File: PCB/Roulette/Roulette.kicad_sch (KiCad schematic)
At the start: 277 parts, among them J1 USB-PROG, J2 Shelly, J3 Conn_01x03, J3 JST-PH-SM3-TBT, J4 Conn_01x02, J6 C3001289, Q1 C179347, Q4 CJ2301, SW1 SW_Push, U2 ESP32-S3-MINI-1, U2 ME6211C33M5G-N, U5 TP4054

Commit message: New boards
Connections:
- net VBUS: now also J1.1 (VBUS)
- no-connect marks 28 -> 27
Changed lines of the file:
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@@
   (no_connect (at 236.855 50.8))
   (no_connect (at 215.9 139.065))
-  (no_connect (at 174.625 107.315))
   (no_connect (at 212.725 80.645))
   (no_connect (at 267.335 60.96))
@@
         )
       )
+    )
+  )
+  (symbol (lib_id "power:VBUS") (at 174.625 107.315 270) (unit 1)
+    (in_bom yes) (on_board yes) (dnp no)
+    (property "Reference" "#PWR043" (at 170.815 107.315 0)
+      (effects (font (size 1.27 1.27)) hide)
+    )
+    (property "Value" "VBUS" (at 179.959 107.315 90)
+      (effects (font (size 1.27 1.27)))
+    )
+    (property "Footprint" "" (at 174.625 107.315 0)
+      (effects (font (size 1.27 1.27)) hide)
+    )
+    (property "Datasheet" "" (at 174.625 107.315 0)
+      (effects (font (size 1.27 1.27)) hide)
+    )
+    (pin "1")
+    (instances
+      (project "Watchy"
+        (path "/03039abc-65dd-445c-a352-9e386e1f31aa"
+          (reference "#PWR043") (unit 1)
+        )
+      )
+      (project "Roulette"
+        (path "/46c350bb-7de4-4e81-aafd-4af55e37aab0"
+          (reference "#PWR051") (unit 1)
+        )
+      )

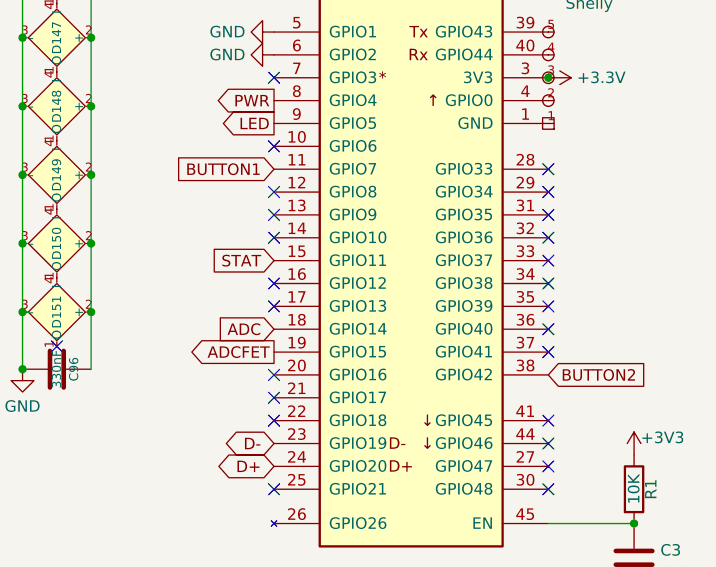
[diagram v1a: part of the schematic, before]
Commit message: Correct btn2
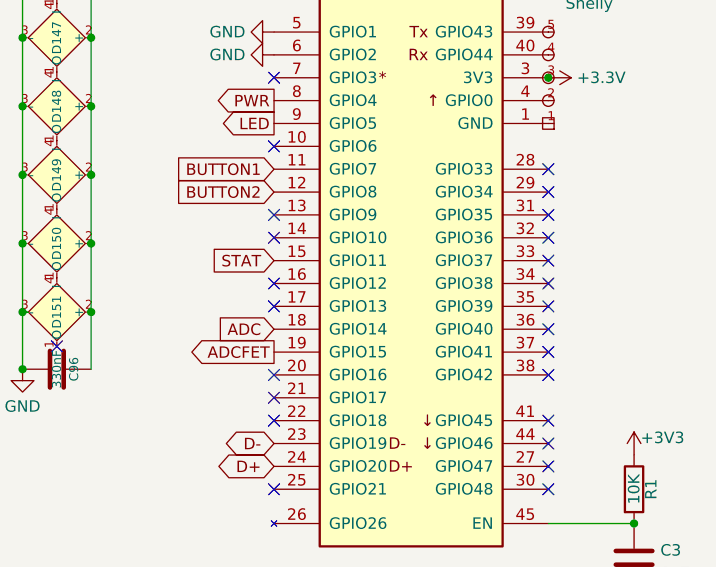
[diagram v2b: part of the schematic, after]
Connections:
- net BUTTON2: now also U2.12 (GPIO8); no longer U2.38 (GPIO42)
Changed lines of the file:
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@@
   (no_connect (at 267.335 66.04))
   (no_connect (at 267.335 78.74))
-  (no_connect (at 236.855 63.5))
+  (no_connect (at 267.335 83.82))
   (wire (pts (xy 208.915 38.735) (xy 208.915 46.355))
     (stroke (width 0) (type default))
@@
     )
   )
-  (global_label "BUTTON2" (shape input) (at 267.335 83.82 0) (fields_autoplaced)
-    (effects (font (size 1.27 1.27)) (justify left))
-    (property "Intersheetrefs" "${INTERSHEET_REFS}" (at 278.0722 83.82 0)
-      (effects (font (size 1.27 1.27)) (justify left) hide)
-    )
-  )
+  (global_label "BUTTON2" (shape input) (at 236.855 63.5 180) (fields_autoplaced)
+    (effects (font (size 1.27 1.27)) (justify right))
+    (property "Intersheetrefs" "${INTERSHEET_REFS}" (at 226.1178 63.5 0)
+      (effects (font (size 1.27 1.27)) (justify right) hide)
+    )
+  )

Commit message: Part IDs
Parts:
- removed J6: C3001289, RevK:USB_C_G_Switch-7082A, symbol RevK:USB_C_Receptacle_G_Switch_7082C
- added J6: USB-C-Socket-V, RevK:USB_C_G_Switch-7082A, symbol RevK:USB-C-Socket-V
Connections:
- net D+: now also J6.A6 (D+), J6.B6 (D+)
- net D-: now also J6.A7 (D-), J6.B7 (D-)
- net GND: now also J6.A1 (GND), J6.A12 (GND), J6.B1 (GND), J6.B12 (GND), J6.S1 (SHIELD)
- net VBUS: now also J6.A4 (VBUS), J6.A9 (VBUS), J6.B4 (VBUS), J6.B9 (VBUS)
- net at R1.2: now also J6.B5 (CC2)
- net at R1.2: now also J6.A5 (CC1)
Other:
- moved on the sheet: R1
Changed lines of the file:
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@@
   (junction (at 31.75 31.115) (diameter 0) (color 0 0 0 0)
   )
+  (junction (at 196.85 148.59) (diameter 0) (color 0 0 0 0)
+  )
   (junction (at 178.435 76.835) (diameter 0) (color 0 0 0 0)
   )
@@
   (junction (at 178.435 24.765) (diameter 0) (color 0 0 0 0)
   )
-  (junction (at 223.52 122.555) (diameter 0) (color 0 0 0 0)
+  (junction (at 223.52 116.84) (diameter 0) (color 0 0 0 0)
   )
   (junction (at -3.175 88.265) (diameter 0) (color 0 0 0 0)
@@
     (stroke (width 0) (type default))
   )
-  (wire (pts (xy 215.9 127.635) (xy 215.9 130.175))
-    (stroke (width 0) (type default))
-  )
   (wire (pts (xy 16.51 28.575) (xy 16.51 33.655))
     (stroke (width 0) (type default))
@@
     (stroke (width 0) (type default))
   )
+  (wire (pts (xy 193.04 148.59) (xy 196.85 148.59))
+    (stroke (width 0) (type default))
+  )
   (wire (pts (xy 24.13 75.565) (xy 24.13 81.915))
     (stroke (width 0) (type default))
@@
     (stroke (width 0) (type default))
   )
-  (wire (pts (xy 215.9 132.715) (xy 215.9 135.255))
-    (stroke (width 0) (type default))
-  )
   (wire (pts (xy 12.7 31.115) (xy 12.7 37.465))
     (stroke (width 0) (type default))
@@
     (stroke (width 0) (type default))
   )
-  (wire (pts (xy 223.52 122.555) (xy 223.52 123.825))
+  (wire (pts (xy 223.52 116.84) (xy 223.52 118.11))
     (stroke (width 0) (type default))
   )
@@
     (stroke (width 0) (type default))
   )
-  (wire (pts (xy 223.52 121.285) (xy 223.52 122.555))
+  (wire (pts (xy 223.52 115.57) (xy 223.52 116.84))
     (stroke (width 0) (type default))
   )
@@
     (stroke (width 0) (type default))
   )
+  (wire (pts (xy 196.85 148.59) (xy 200.66 148.59))
+    (stroke (width 0) (type default))
+  )
   (wire (pts (xy 94.615 46.355) (xy 94.615 53.975))
     (stroke (width 0) (type default))
@@
     )
   )
-  (global_label "D+" (shape bidirectional) (at 215.9 133.985 0) (fields_autoplaced)
+  (global_label "D+" (shape bidirectional) (at 215.9 128.27 0) (fields_autoplaced)
     (effects (font (size 1.27 1.27)) (justify left))
-    (property "Intersheetrefs" "${INTERSHEET_REFS}" (at 221.9465 133.985 0)
+    (property "Intersheetrefs" "${INTERSHEET_REFS}" (at 221.9465 128.27 0)
       (effects (font (size 1.27 1.27)) (justify left) hide)
     )
@@
     )
   )
-  (global_label "D-" (shape bidirectional) (at 215.9 128.905 0) (fields_autoplaced)
+  (global_label "D-" (shape bidirectional) (at 215.9 125.73 0) (fields_autoplaced)
     (effects (font (size 1.27 1.27)) (justify left))
-    (property "Intersheetrefs" "${INTERSHEET_REFS}" (at 221.9465 128.905 0)
+    (property "Intersheetrefs" "${INTERSHEET_REFS}" (at 221.9465 125.73 0)
       (effects (font (size 1.27 1.27)) (justify left) hide)
     )
@@
     )
   )
-  (symbol (lib_id "power:GND") (at 223.52 122.555 90) (unit 1)
+  (symbol (lib_id "power:GND") (at 223.52 116.84 90) (unit 1)
     (in_bom yes) (on_board yes) (dnp no)
-    (property "Reference" "#PWR045" (at 229.87 122.555 0)
+    (property "Reference" "#PWR045" (at 229.87 116.84 0)
       (effects (font (size 1.27 1.27)) hide)
     )
-    (property "Value" "GND" (at 228.6 122.555 90)
+    (property "Value" "GND" (at 228.6 116.84 90)
       (effects (font (size 1.27 1.27)))
     )
-    (property "Footprint" "" (at 223.52 122.555 0)
+    (property "Footprint" "" (at 223.52 116.84 0)
       (effects (font (size 1.27 1.27)) hide)
     )
-    (property "Datasheet" "" (at 223.52 122.555 0)
+    (property "Datasheet" "" (at 223.52 116.84 0)
       (effects (font (size 1.27 1.27)) hide)
     )
@@
     )
   )
-  (symbol (lib_id "Device:R") (at 219.71 123.825 270) (unit 1)
+  (symbol (lib_id "Device:R") (at 219.71 118.11 270) (unit 1)
     (in_bom yes) (on_board yes) (dnp no)
-    (property "Reference" "R1" (at 219.71 126.365 90)
+    (property "Reference" "R1" (at 219.71 120.65 90)
       (effects (font (size 1.27 1.27)))
     )
-    (property "Value" "5K1" (at 219.71 123.825 90)
+    (property "Value" "5K1" (at 219.71 118.11 90)
       (effects (font (size 1.27 1.27)))
     )
-    (property "Footprint" "RevK:R_0402" (at 219.71 122.047 90)
+    (property "Footprint" "RevK:R_0402" (at 219.71 116.332 90)
       (effects (font (size 1.27 1.27)) hide)
     )
-    (property "Datasheet" "~" (at 219.71 123.825 0)
+    (property "Datasheet" "~" (at 219.71 118.11 0)
       (effects (font (size 1.27 1.27)) hide)
     )
@@
     )
   )
+  (symbol (lib_id "RevK:USB-C-Socket-V") (at 200.66 125.73 0) (unit 1)
+    (in_bom yes) (on_board yes) (dnp no) (fields_autoplaced)
+    (property "Reference" "J6" (at 200.66 103.8057 0)
+      (effects (font (size 1.27 1.27)))
+    )
+    (property "Value" "USB-C-Socket-V" (at 200.66 106.2299 0)
+      (effects (font (size 1.27 1.27)))
+    )
+    (property "Footprint" "RevK:USB_C_G_Switch-7082A" (at 200.66 105.41 0)
+      (effects (font (size 1.27 1.27)) hide)
+    )
+    (property "Datasheet" "" (at 200.66 102.87 0)
+      (effects (font (size 1.27 1.27)) hide)
+    )
+    (property "LCSC Part #" "C709357" (at 200.66 125.73 0)
+      (effects (font (size 1.27 1.27)) hide)
+    )
+    (pin "A1")
+    (pin "A12")
+    (pin "A4")
+    (pin "A5")
+    (pin "A6")
+    (pin "A7")
+    (pin "A8")
+    (pin "A9")
+    (pin "B1")
+    (pin "B12")
+    (pin "B4")
+    (pin "B5")
+    (pin "B6")
+    (pin "B7")
+    (pin "B8")
+    (pin "B9")
+    (pin "S1")
+    (instances
+      (project "Roulette"
+        (path "/46c350bb-7de4-4e81-aafd-4af55e37aab0"
+          (reference "J6") (unit 1)
+        )
+      )
+    )
+  )
   (symbol (lib_id "Device:R") (at 251.46 131.445 0) (unit 1)
     (in_bom yes) (on_board yes) (dnp no)
@@
     )
   )
-  (symbol (lib_id "RevK:USB_C_Receptacle_G_Switch_7082C") (at 200.66 125.73 0) (unit 1)
-    (in_bom yes) (on_board yes) (dnp no) (fields_autoplaced)
-    (property "Reference" "J6" (at 200.66 106.2299 0)
-      (effects (font (size 1.27 1.27)))
-    )
-    (property "Value" "C3001289" (at 200.66 106.2299 0)
-      (effects (font (size 1.27 1.27)) hide)
-    )
-    (property "Footprint" "RevK:USB_C_G_Switch-7082A" (at 204.47 125.73 0)
-      (effects (font (size 1.27 1.27)) hide)
-    )
-    (property "Datasheet" "https://www.usb.org/sites/default/files/documents/usb_type-c.zip" (at 204.47 125.73 0)
-      (effects (font (size 1.27 1.27)) hide)
-    )
-    (property "LCSC Part #" "C3001289" (at 200.66 125.73 0)
-      (effects (font (size 1.27 1.27)) hide)
-    )
-    (pin "A1")
-    (pin "A12")
-    (pin "A4")
-    (pin "A5")
-    (pin "A6")
-    (pin "A7")
-    (pin "A8")
-    (pin "A9")
-    (pin "B1")
-    (pin "B12")
-    (pin "B4")
-    (pin "B5")
-    (pin "B6")
-    (pin "B7")
-    (pin "B8")
-    (pin "B9")
-    (instances
-      (project "Roulette"
-        (path "/46c350bb-7de4-4e81-aafd-4af55e37aab0"
-          (reference "J6") (unit 1)
-        )
-      )
-    )
-  )
   (symbol (lib_id "Device:C") (at 62.23 81.915 270) (mirror x) (unit 1)
     (in_bom yes) (on_board yes) (dnp no)
@@
     )
   )
-  (symbol (lib_id "power:GND") (at 199.39 148.59 0) (unit 1)
+  (symbol (lib_id "power:GND") (at 196.85 148.59 0) (unit 1)
     (in_bom yes) (on_board yes) (dnp no)
-    (property "Reference" "#PWR021" (at 199.39 154.94 0)
+    (property "Reference" "#PWR021" (at 196.85 154.94 0)
       (effects (font (size 1.27 1.27)) hide)
     )
-    (property "Value" "GND" (at 199.39 153.67 90)
+    (property "Value" "GND" (at 196.85 153.67 90)
       (effects (font (size 1.27 1.27)))
     )
-    (property "Footprint" "" (at 199.39 148.59 0)
+    (property "Footprint" "" (at 196.85 148.59 0)
       (effects (font (size 1.27 1.27)) hide)
     )
-    (property "Datasheet" "" (at 199.39 148.59 0)
+    (property "Datasheet" "" (at 196.85 148.59 0)
       (effects (font (size 1.27 1.27)) hide)
     )
@@
     )
   )
-  (symbol (lib_id "Device:R") (at 219.71 121.285 270) (unit 1)
+  (symbol (lib_id "Device:R") (at 219.71 115.57 270) (unit 1)
     (in_bom yes) (on_board yes) (dnp no)
-    (property "Reference" "R1" (at 219.71 118.745 90)
+    (property "Reference" "R1" (at 219.71 113.03 90)
       (effects (font (size 1.27 1.27)))
     )
-    (property "Value" "5K1" (at 219.71 121.285 90)
+    (property "Value" "5K1" (at 219.71 115.57 90)
       (effects (font (size 1.27 1.27)))
     )
-    (property "Footprint" "RevK:R_0402" (at 219.71 119.507 90)
+    (property "Footprint" "RevK:R_0402" (at 219.71 113.792 90)
       (effects (font (size 1.27 1.27)) hide)
     )
-    (property "Datasheet" "~" (at 219.71 121.285 0)
+    (property "Datasheet" "~" (at 219.71 115.57 0)
       (effects (font (size 1.27 1.27)) hide)
     )

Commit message: Library update
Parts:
- J6: footprint RevK:USB_C_G_Switch-7082A -> RevK:USB-C-Socket-V; LCSC Part # C709357 -> C3001289
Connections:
- net GND: no longer J6.S1 (SHIELD)
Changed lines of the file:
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@@
   (junction (at 31.75 31.115) (diameter 0) (color 0 0 0 0)
   )
-  (junction (at 196.85 148.59) (diameter 0) (color 0 0 0 0)
-  )
   (junction (at 178.435 76.835) (diameter 0) (color 0 0 0 0)
   )
@@
     (stroke (width 0) (type default))
   )
-  (wire (pts (xy 193.04 148.59) (xy 196.85 148.59))
-    (stroke (width 0) (type default))
-  )
   (wire (pts (xy 24.13 75.565) (xy 24.13 81.915))
     (stroke (width 0) (type default))
@@
     (stroke (width 0) (type default))
   )
-  (wire (pts (xy 196.85 148.59) (xy 200.66 148.59))
-    (stroke (width 0) (type default))
-  )
   (wire (pts (xy 94.615 46.355) (xy 94.615 53.975))
     (stroke (width 0) (type default))
@@
       (effects (font (size 1.27 1.27)))
     )
-    (property "Footprint" "RevK:USB_C_G_Switch-7082A" (at 200.66 105.41 0)
+    (property "Footprint" "RevK:USB-C-Socket-V" (at 200.66 105.41 0)
       (effects (font (size 1.27 1.27)) hide)
     )
@@
       (effects (font (size 1.27 1.27)) hide)
     )
-    (property "LCSC Part #" "C709357" (at 200.66 125.73 0)
+    (property "LCSC Part #" "C3001289" (at 200.66 125.73 0)
       (effects (font (size 1.27 1.27)) hide)
     )
@@
     (pin "B8")
     (pin "B9")
-    (pin "S1")
     (instances
       (project "Roulette"
@@
     )
   )
-  (symbol (lib_id "power:GND") (at 196.85 148.59 0) (unit 1)
+  (symbol (lib_id "power:GND") (at 200.66 148.59 0) (unit 1)
     (in_bom yes) (on_board yes) (dnp no)
-    (property "Reference" "#PWR021" (at 196.85 154.94 0)
+    (property "Reference" "#PWR021" (at 200.66 154.94 0)
       (effects (font (size 1.27 1.27)) hide)
     )
-    (property "Value" "GND" (at 196.85 153.67 90)
+    (property "Value" "GND" (at 200.66 153.67 90)
       (effects (font (size 1.27 1.27)))
     )
-    (property "Footprint" "" (at 196.85 148.59 0)
+    (property "Footprint" "" (at 200.66 148.59 0)
       (effects (font (size 1.27 1.27)) hide)
     )
-    (property "Datasheet" "" (at 196.85 148.59 0)
+    (property "Datasheet" "" (at 200.66 148.59 0)
       (effects (font (size 1.27 1.27)) hide)
     )

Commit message: Tidy
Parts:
- removed Q1: C179347, RevK:SOT-323_SC-70, symbol Device:Q_PMOS_GSD
- removed R1: 10K, RevK:R_0402, symbol Device:R
- removed U5: TP4054, RevK:SOT-23-5, symbol Watchy-rescue:MCP73831-2-OT-Battery_Management
- added D153, D154: ~, RevK:DFN1006-2L, symbol RevK:ES05D1MC10
- added U2: TP4054, RevK:SOT-23-5, symbol RevK:TP4054
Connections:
- net BUTTON1: now also D153.2
- net BUTTON2: now also D154.2
- net GND: now also D153.1, D154.1, U2.2 (VSS)
- net STAT: now also U2.1 (STAT)
- net VBAT: now also R12.1, U2.3 (VBAT)
- net VBUS: now also U2.4 (VDD)
- net at R15.2: now also U2.5 (PROG)
- net +3V3 renamed +3.3V
- net ADCFET: no longer names the net of U2.19 (GPIO15)
- net VCC renamed VLED
- no-connect marks 27 -> 26
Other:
- moved on the sheet: C3, D4, Q4, R1, R14, R15, U2

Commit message: Broken
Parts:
- renumbered C12 to C100, C1 to C97, C2 to C98, C3 to C99, D4 to D152, J3 to J5, Q4 to Q2, R13 to R10, R1 to R2, R1 to R3, R1 to R4, R1 to R5, R15 to R6, R14 to R7, R1 to R8, R12 to R9, SW1 to SW2, U2 to U1, U2 to U3

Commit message: PCB Update
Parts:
- C1, C10, C11, C12, C13, C14, C15, C16, C17, C18, C19, C2, C20, C21, C22, C23, C24, C25, C26, C27, C28, C29, C3, C30, C31, C32, C33, C34, C35, C36, C37, C38, C39, C4, C40, C41, C42, C43, C44, C45, C46, C47, C48, C49, C5, C50, C51, C52, C53, C54, C55, C56, C57, C58, C59, C6, C60, C61, C62, C63, C64, C65, C66, C67, C68, C69, C7, C70, C71, C72, C73, C74, C75, C76, C77, C78, C79, C8, C80, C81, C82, C83, C84, C85, C86, C87, C88, C89, C9, C90, C91, C92, C93, C94, C95, C96, C97, C98, C99: footprint RevK:C_0402 -> (none)
- C100: footprint RevK:C_0805 -> (none)
- D1, D10, D100, D101, D102, D103, D104, D105, D106, D107, D108, D109, D11, D110, D111, D112, D113, D114, D115, D116, D117, D118, D119, D12, D120, D121, D122, D123, D124, D125, D126, D127, D128, D129, D13, D130, D131, D132, D133, D134, D135, D136, D137, D138, D139, D14, D140, D141, D142, D143, D144, D145, D146, D147, D148, D149, D15, D150, D151, D16, D17, D18, D19, D2, D20, D21, D22, D23, D24, D25, D26, D27, D28, D29, D3, D30, D31, D32, D33, D34, D35, D36, D37, D38, D39, D4, D40, D41, D42, D43, D44, D45, D46, D47, D48, D49, D5, D50, D51, D52, D53, D54, D55, D56, D57, D58, D59, D6, D60, D61, D62, D63, D64, D65, D66, D67, D68, D69, D7, D70, D71, D72, D73, D74, D75, D76, D77, D78, D79, D8, D80, D81, D82, D83, D84, D85, D86, D87, D88, D89, D9, D90, D91, D92, D93, D94, D95, D96, D97, D98, D99: footprint RevK:SMD1010 -> (none); LCSC Part # C5349953 -> (none); MPN (none) -> C5349953
- D152: footprint RevK:D_SOD-123 -> (none)
- D153, D154: value ~ -> (none); LCSC Part # C5137770 -> (none); MPN (none) -> C5137770
- J3: footprint RevK:3-PADS -> (none)
- J4: footprint RevK:2-PADS -> (none)
- J5: footprint Connector_JST:JST_PH_B2B-PH-SM4-TB_1x02-1MP_P2.00mm_Vertical -> (none); LCSC Part # C265003 -> (none)
- J6: LCSC Part # C3001289 -> (none); MPN (none) -> C3001289
- Q1: footprint RevK:SOT-323_SC-70 -> (none); LCSC Part # C179347 -> (none); Note Any P-Channel SOT323 that does 3.3V/0.5A -> (none)
- Q2: JLCPCB Rotation Offset 180 -> (none); LCSC Part # C5224170 -> (none)
- R1, R10, R2, R3, R4, R5, R6, R7, R8, R9: footprint RevK:R_0402 -> (none)
- SW1, SW2: footprint RevK:TS-1092S-B3D2-G -> (none); LCSC Part # C520860 -> (none)
- U1: LCSC Part # C3013941 -> (none); MPN (none) -> C3013941
- U2: JLCPCB Rotation Offset 180 -> (none); LCSC Part # C668215 -> (none); MPN (none) -> C668215
- U3: JLCPCB Rotation Offset -90 -> (none); LCSC Part # C82942 -> (none)
